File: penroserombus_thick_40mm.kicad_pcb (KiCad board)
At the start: 2 copper layers, 52.4 x 38 mm, 21 parts, among them J1 Conn_01x03_Female, J2 Conn_01x03_Female, J3 Conn_01x03_Male, J4 Conn_01x03_Male, M2.1 MountingHole_2.1mm, SW1 SW_DPDT_x2

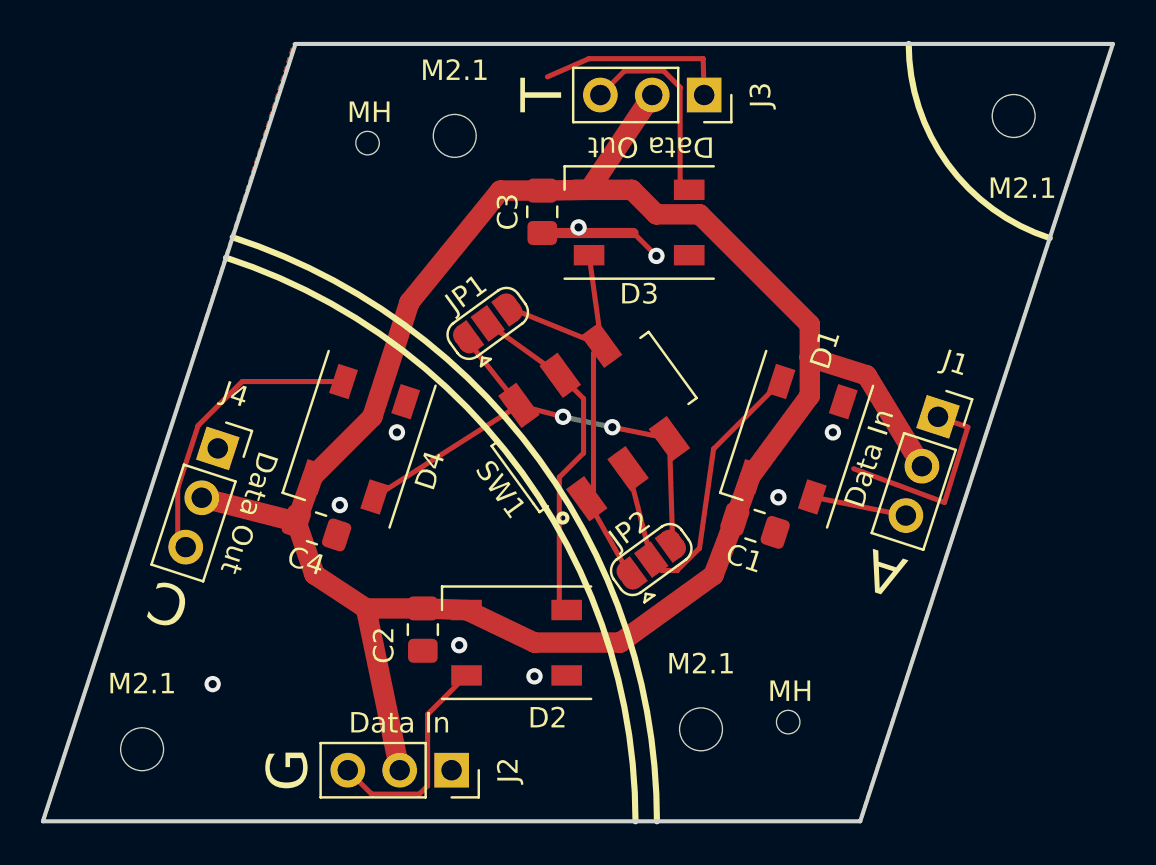
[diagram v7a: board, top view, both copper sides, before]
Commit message: shifted ports  on penrose rhombi to enforce all matching rules. fixed flipped ports on penrose dart.
going to make new gerbers later.
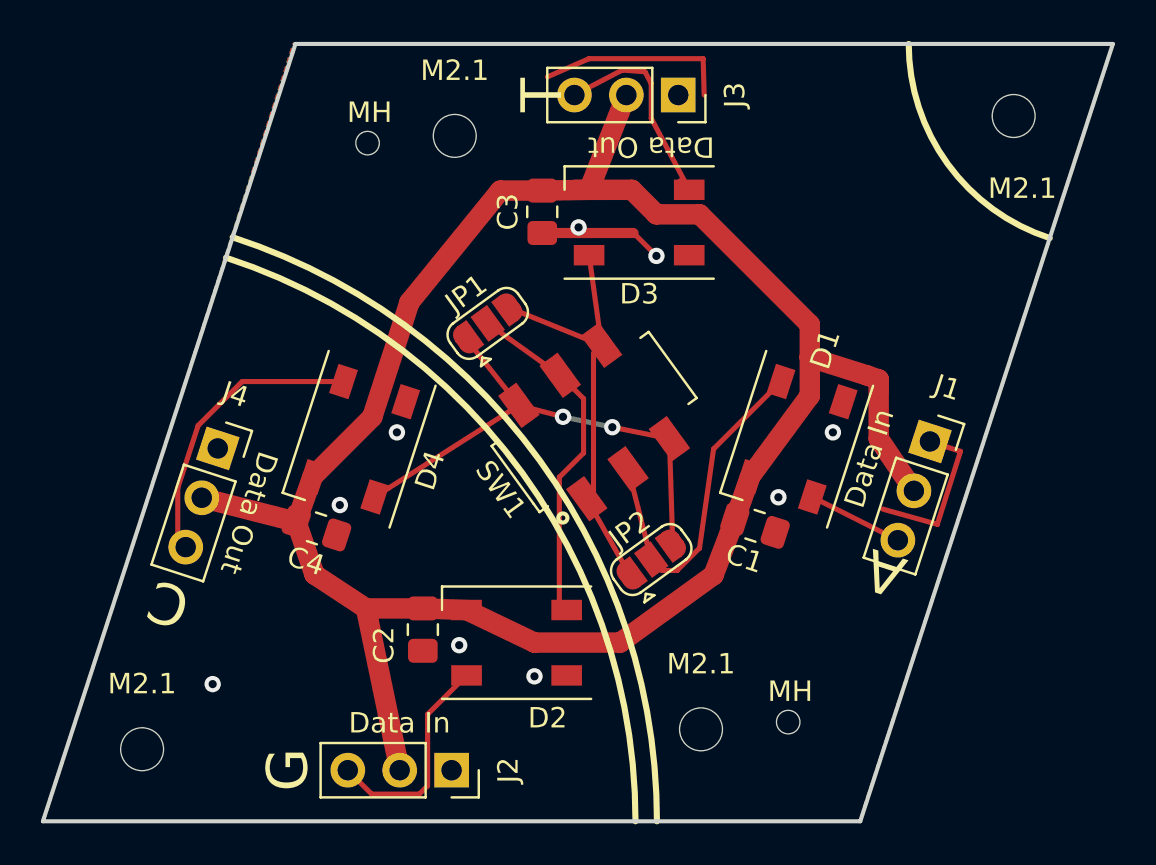
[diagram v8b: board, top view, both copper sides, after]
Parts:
- moved J1 1.27 mm to (164.3, 95.4)
- moved J3 1.27 mm to (151.9, 78.5)
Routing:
- net GND: track 25.8 -> 23.7 mm
- net VCC: track 102.0 -> 102.8 mm
- net Net-(D3-Pad4): track 9.92 -> 10.7 mm
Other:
- board text added: "Gnd Vcc Data"
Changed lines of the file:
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@@
   (general
     (thickness 1.6)
-    (drawings 28)
-    (tracks 87)
+    (drawings 32)
+    (tracks 90)
     (zones 0)
     (modules 21)
@@
     )
   )
-  (module Connector_PinSocket_2.54mm:PinSocket_1x03_P2.54mm_Vertical locked (layer F.Cu)
-    (at 164.654318 94.234587 342)
+  (module Connector_PinSocket_2.54mm:PinSocket_1x03_P2.54mm_Vertical (layer F.Cu)
+    (at 164.261635 95.440951 342)
     (descr "Through hole straight socket strip, 1x03, 2.54mm pitch, single row (from Kicad 4.0.7), script generated")
     (tags "Through hole socket strip THT 1x03 2.54mm single row")
@@
     )
   )
-  (module Connector_PinSocket_2.54mm:PinSocket_1x03_P2.54mm_Vertical locked (layer F.Cu)
-    (at 153.2123 78.486 270)
+  (module Connector_PinSocket_2.54mm:PinSocket_1x03_P2.54mm_Vertical (layer F.Cu)
+    (at 151.943635 78.486676 270)
     (descr "Through hole straight socket strip, 1x03, 2.54mm pitch, single row (from Kicad 4.0.7), script generated")
     (tags "Through hole socket strip THT 1x03 2.54mm single row")
@@
     )
   )
+  (gr_text "Gnd\nVcc\nData" (at 129.5908 98.679 342) (layer B.SilkS)
+    (effects (font (size 1.5 1.5) (thickness 0.375)) (justify right mirror))
+  )
+  (gr_text "Gnd\nVcc\nData" (at 162.7886 96.3422 342) (layer B.SilkS)
+    (effects (font (size 1.5 1.5) (thickness 0.375)) (justify left mirror))
+  )
+  (gr_text "Gnd\nVcc\nData" (at 138.2776 110.5408 270) (layer B.SilkS)
+    (effects (font (size 1.5 1.5) (thickness 0.375)) (justify left mirror))
+  )
+  (gr_text "Gnd\nVcc\nData" (at 150.749 79.4512 270) (layer B.SilkS)
+    (effects (font (size 1.5 1.5) (thickness 0.375)) (justify right mirror))
+  )
   (gr_text "Data In" (at 161.29 96.266 72) (layer F.SilkS)
     (effects (font (size 1 1) (thickness 0.15)))
@@
   (segment (start 155.458843 97.167356) (end 154.715279 99.247395) (width 1) (layer F.Cu) (net 1))
   (segment (start 145.288 83.1635) (end 147.581513 83.125141) (width 1) (layer F.Cu) (net 1))
-  (segment (start 147.581513 83.125141) (end 150.6723 78.486) (width 1) (layer F.Cu) (net 1))
   (segment (start 139.446 103.6105) (end 136.662962 103.6105) (width 1) (layer F.Cu) (net 1))
   (segment (start 158.380327 89.713953) (end 152.991516 84.325142) (width 1) (layer F.Cu) (net 1))
@@
   (segment (start 133.252279 99.374395) (end 134.142017 101.950983) (width 1) (layer F.Cu) (net 1))
   (segment (start 134.142017 101.950983) (end 136.662962 103.6105) (width 1) (layer F.Cu) (net 1))
-  (segment (start 163.869415 96.650271) (end 161.163 92.202) (width 1) (layer F.Cu) (net 1))
   (segment (start 161.163 92.202) (end 158.380327 91.324327) (width 1) (layer F.Cu) (net 1))
   (segment (start 158.380327 91.324327) (end 158.380327 89.713953) (width 1) (layer F.Cu) (net 1))
@@
   (segment (start 149.098 105.283) (end 153.67 101.981) (width 1) (layer F.Cu) (net 1))
   (segment (start 153.67 101.981) (end 154.715279 99.247395) (width 1) (layer F.Cu) (net 1))
+  (segment (start 149.403635 78.486676) (end 147.581513 83.125141) (width 1) (layer F.Cu) (net 1))
+  (segment (start 163.476732 97.856635) (end 161.75228 95.3008) (width 1) (layer F.Cu) (net 1))
+  (segment (start 161.75228 95.3008) (end 161.754736 92.405284) (width 1) (layer F.Cu) (net 1))
+  (segment (start 161.754736 92.405284) (end 161.163 92.202) (width 1) (layer F.Cu) (net 1))
   (via (at 141.224 105.41) (size 0.8) (drill 0.4) (layers F.Cu B.Cu) (net 2))
   (via (at 138.176 94.996) (size 0.8) (drill 0.4) (layers F.Cu B.Cu) (net 2))
@@
   (segment (start 149.7545 85.2385) (end 150.876 86.36) (width 0.25) (layer F.Cu) (net 2))
   (segment (start 145.288 85.2385) (end 149.7545 85.2385) (width 0.5) (layer F.Cu) (net 2))
-  (segment (start 164.654318 94.234587) (end 166.116 94.742) (width 0.25) (layer F.Cu) (net 2))
-  (segment (start 166.116 94.742) (end 164.973 98.425) (width 0.25) (layer F.Cu) (net 2))
-  (segment (start 164.973 98.425) (end 160.528 96.774) (width 0.25) (layer F.Cu) (net 2))
-  (segment (start 163.084512 99.065954) (end 158.502224 98.156211) (width 0.25) (layer F.Cu) (net 3))
+  (segment (start 164.261635 95.440951) (end 165.75532 95.92564) (width 0.25) (layer F.Cu) (net 2))
+  (segment (start 165.75532 95.92564) (end 164.62248 99.49434) (width 0.25) (layer F.Cu) (net 2))
+  (segment (start 164.62248 99.49434) (end 161.94532 98.74758) (width 0.25) (layer F.Cu) (net 2))
+  (segment (start 162.691829 100.272318) (end 158.502224 98.156211) (width 0.25) (layer F.Cu) (net 3))
   (segment (start 149.488493 96.773473) (end 150.622 101.219) (width 0.25) (layer F.Cu) (net 4))
   (segment (start 153.673275 95.80693) (end 156.973026 92.507179) (width 0.25) (layer F.Cu) (net 4))
@@
   (segment (start 147.581513 86.325141) (end 148.190049 90.733064) (width 0.25) (layer F.Cu) (net 7))
   (segment (start 152.037299 82.680927) (end 152.481513 83.125141) (width 0.25) (layer F.Cu) (net 8))
-  (segment (start 152.037299 78.111997) (end 152.037299 82.680927) (width 0.25) (layer F.Cu) (net 8))
-  (segment (start 151.236301 77.310999) (end 152.037299 78.111997) (width 0.25) (layer F.Cu) (net 8))
-  (segment (start 149.307301 77.310999) (end 151.236301 77.310999) (width 0.25) (layer F.Cu) (net 8))
-  (segment (start 148.1323 78.486) (end 149.307301 77.310999) (width 0.25) (layer F.Cu) (net 8))
+  (segment (start 152.481513 83.125141) (end 150.622 79.629) (width 0.25) (layer F.Cu) (net 8))
+  (segment (start 149.1996 77.2668) (end 146.863635 78.486676) (width 0.25) (layer F.Cu) (net 8))
+  (segment (start 150.313814 77.346386) (end 150.622 77.9272) (width 0.25) (layer F.Cu) (net 8))
+  (segment (start 150.622 79.629) (end 150.622 77.9272) (width 0.25) (layer F.Cu) (net 8))
+  (segment (start 150.313814 77.346386) (end 149.1996 77.2668) (width 0.25) (layer F.Cu) (net 8))
   (segment (start 130.605662 92.507179) (end 135.561695 92.507179) (width 0.25) (layer F.Cu) (net 9))
   (segment (start 127.839795 100.611039) (end 127.449697 100.220941) (width 0.25) (layer F.Cu) (net 9))
